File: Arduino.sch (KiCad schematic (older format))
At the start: 0 parts

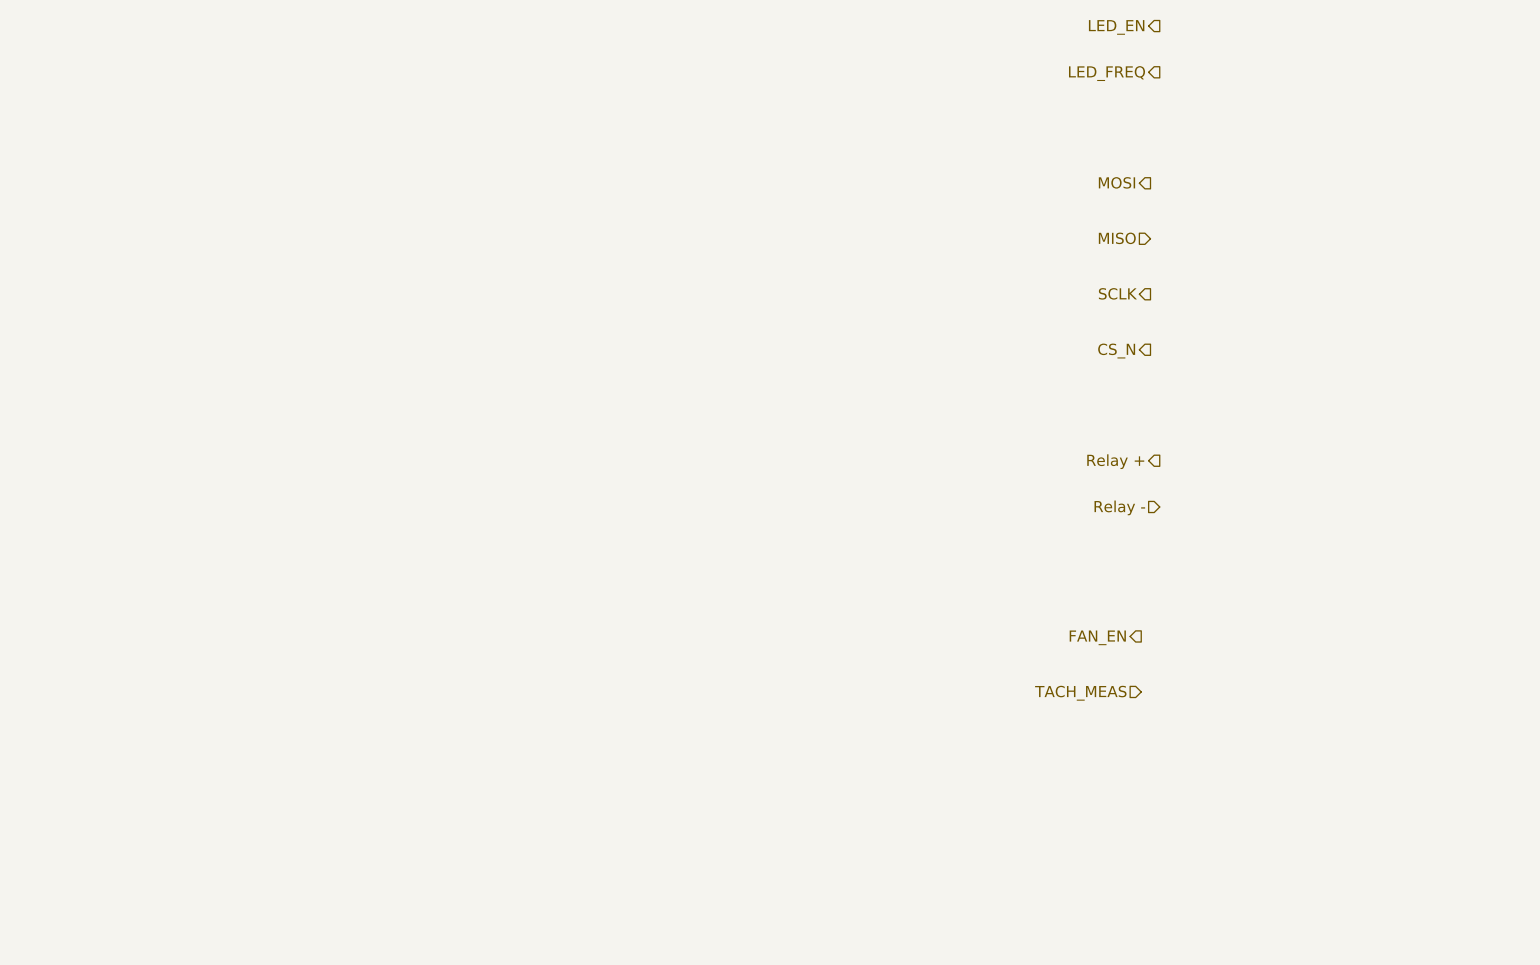
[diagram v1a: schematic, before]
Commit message: M3 U8
Arduino Module.   My Arduino Pin numbering does not matches Chris'.  I
believe he missed one in the video
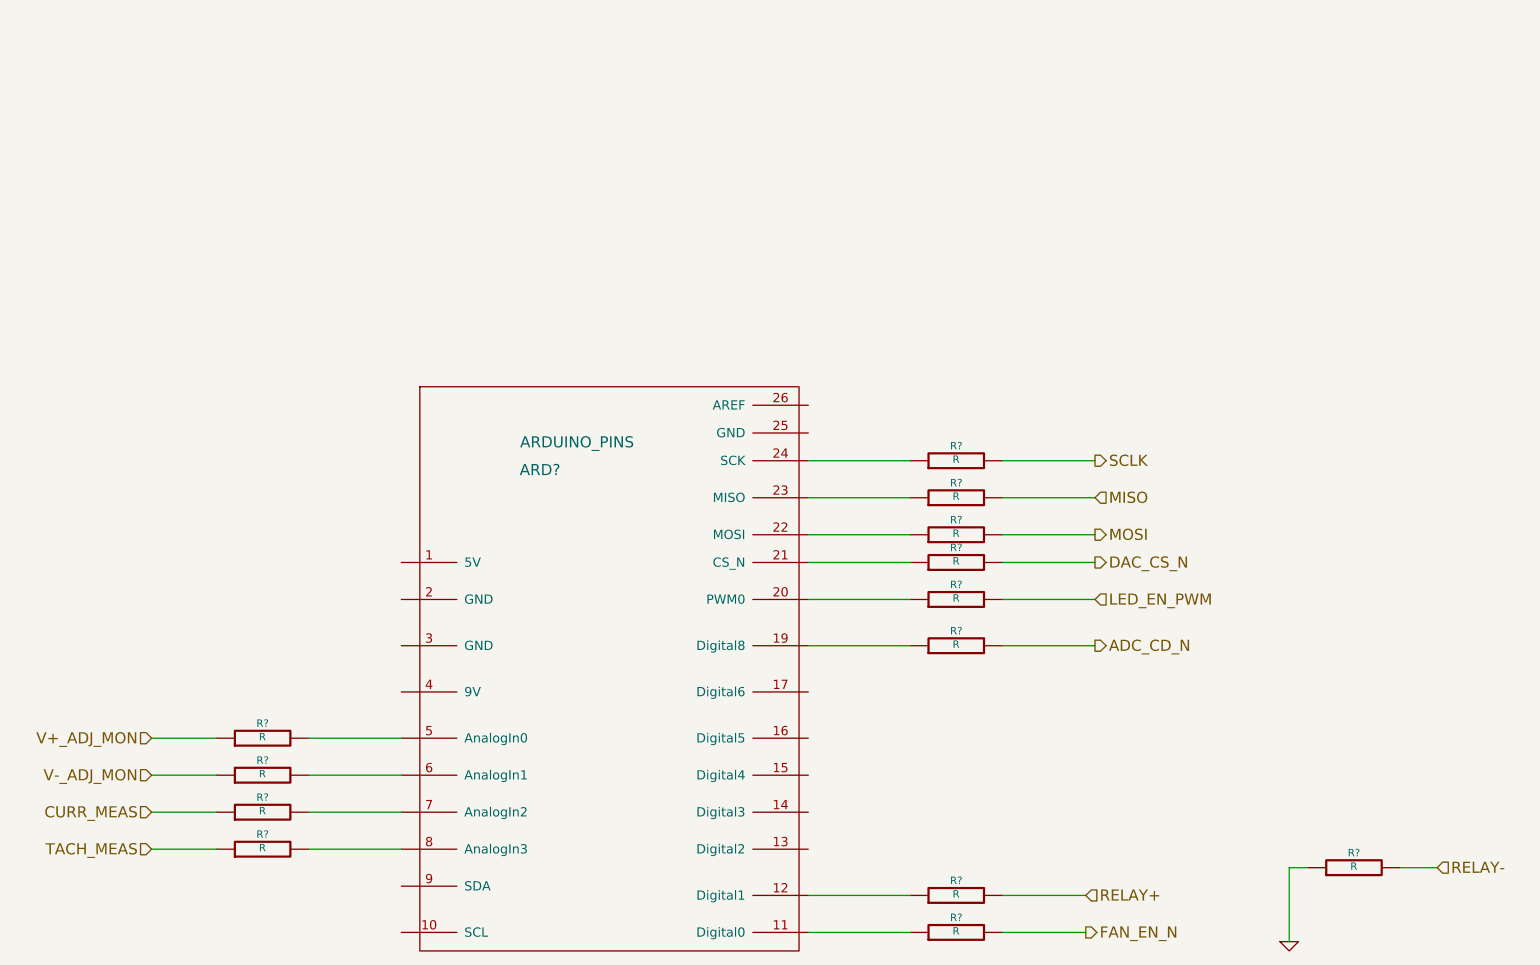
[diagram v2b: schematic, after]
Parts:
- added ARD?: ARDUINO_PINS, symbol ARDUINO_PINS
- added R? (x13): R, ~, symbol R
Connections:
- net MISO: now also R?.2
- net MOSI: now also R?.2
- net SCLK: now also R?.2
- net TACH_MEAS: now also R?.1
- new net: ARD?.11 (Digital0), R?.1
- new net: ARD?.12 (Digital1), R?.1
- new net: ARD?.19 (Digital8), R?.1
- new net: ARD?.20 (PWM0), R?.1
- new net: ARD?.21 (CS_N), R?.1
- new net: ARD?.22 (MOSI), R?.1
- new net: ARD?.23 (MISO), R?.1
- new net: ARD?.24 (SCK), R?.1
- new net: ARD?.5 (AnalogIn0), R?.2
- new net: ARD?.6 (AnalogIn1), R?.2
- new net: ARD?.7 (AnalogIn2), R?.2
- new net: ARD?.8 (AnalogIn3), R?.2
- new net ADC_CD_N: R?.2
- new net CURR_MEAS: R?.1
- new net DAC_CS_N: R?.2
- new net FAN_EN_N: R?.2
- new net GND: R?.1
- new net LED_EN_PWM: R?.2
- new net RELAY+: R?.2
- new net RELAY-: R?.2
- new net V+_ADJ_MON: R?.1
- new net V-_ADJ_MON: R?.1

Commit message: M3 U9
Revisiting the Current/Fan Module
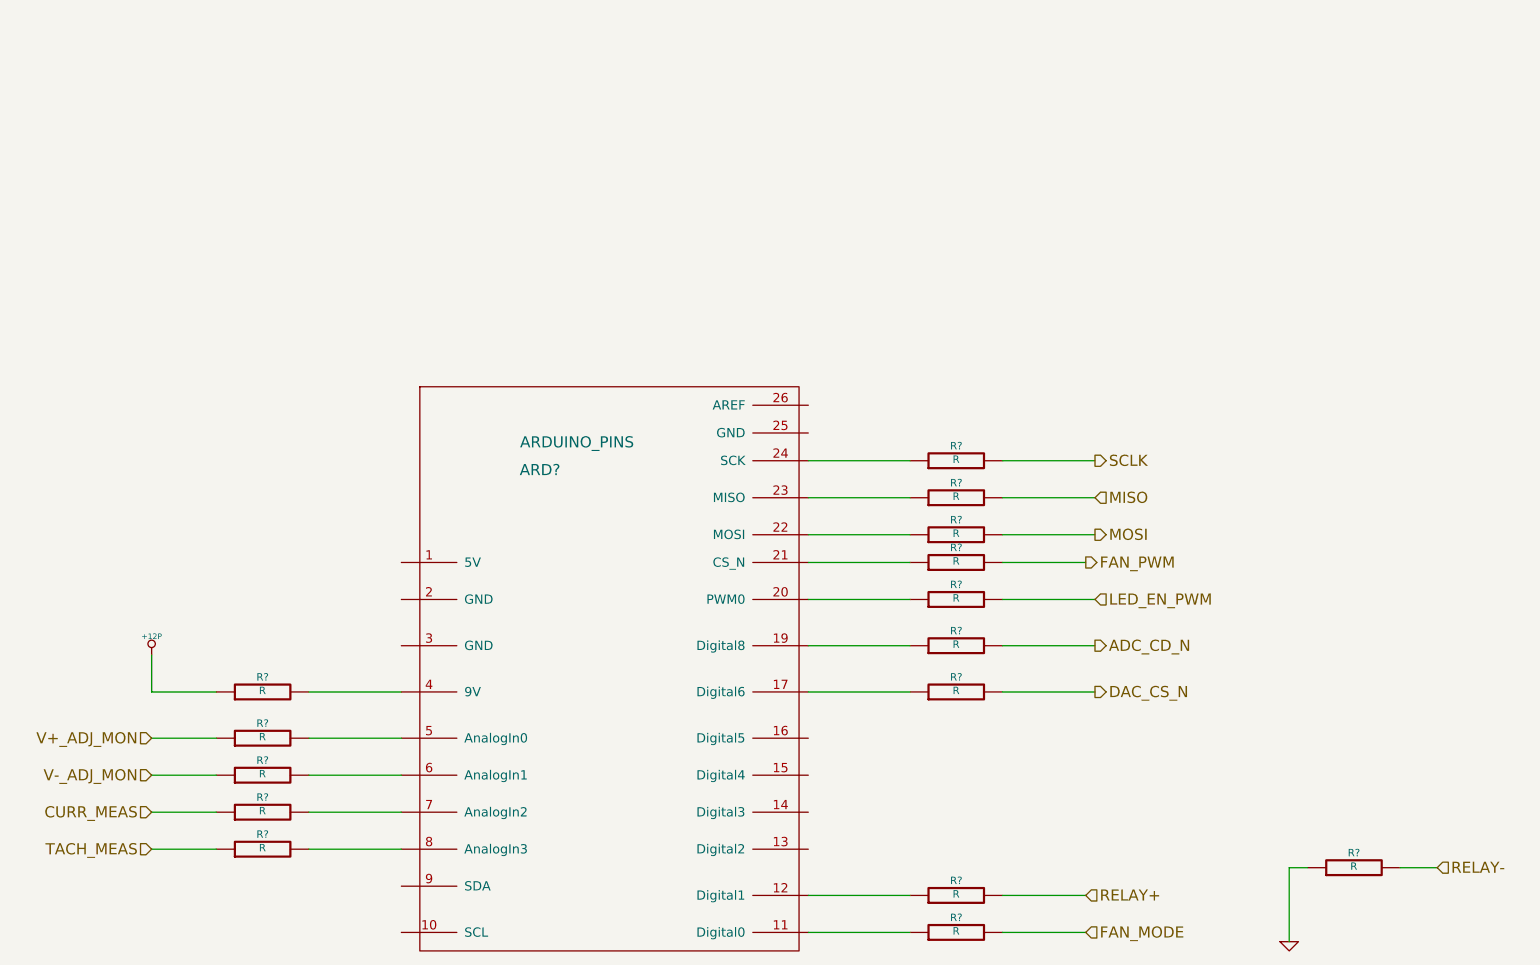
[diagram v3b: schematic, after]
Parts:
- added R? (x2): R, ~, symbol R
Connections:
- net at ARD?.11 (Digital0): now also R?.1; no longer R?.1
- net at ARD?.17 (Digital6): now also R?.1
- net at ARD?.21 (CS_N): now also R?.1; no longer R?.1
- net at ARD?.4 (9V): now also R?.2
- net FAN_EN_N renamed FAN_PWM
- new net +12P: R?.1
- new net FAN_MODE: R?.2
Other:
- moved on the sheet: R?
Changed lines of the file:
@@
 Text HLabel 6750 3850 2    60   Output ~ 0
 SCLK
-Text HLabel 6750 4400 2    60   Output ~ 0
+Text HLabel 6750 5100 2    60   Output ~ 0
 DAC_CS_N
-Text HLabel 6700 6400 2    60   Output ~ 0
-FAN_EN_N
+Text HLabel 6700 4400 2    60   Output ~ 0
+FAN_PWM
 Text HLabel 1650 5950 0    60   Input ~ 0
 TACH_MEAS
@@
 	6250 4250 6750 4250
 Wire Wire Line
-	6750 4400 6250 4400
+	6750 5100 6250 5100
 Wire Wire Line
 	3000 5950 2500 5950
@@
 L R R?
 U 1 1 52FEF63C
-P 6000 6400
-F 0 "R?" V 6080 6400 40  0000 C CNN
-F 1 "R" V 6007 6401 40  0000 C CNN
-F 2 "~" V 5930 6400 30  0000 C CNN
-F 3 "~" H 6000 6400 30  0000 C CNN
-	1    6000 6400
-	0    -1   -1   0
-$EndComp
-Wire Wire Line
-	6700 6400 6250 6400
-Wire Wire Line
-	5750 6400 5200 6400
+P 6000 4400
+F 0 "R?" V 6080 4400 40  0000 C CNN
+F 1 "R" V 6007 4401 40  0000 C CNN
+F 2 "~" V 5930 4400 30  0000 C CNN
+F 3 "~" H 6000 4400 30  0000 C CNN
+	1    6000 4400
+	0    -1   -1   0
+$EndComp
+Wire Wire Line
+	6700 4400 6250 4400
+Wire Wire Line
+	5750 4400 5200 4400
 $Comp
 L R R?
@@
 L R R?
 U 1 1 52FF6371
-P 6000 4400
-F 0 "R?" V 6080 4400 40  0000 C CNN
-F 1 "R" V 6007 4401 40  0000 C CNN
-F 2 "~" V 5930 4400 30  0000 C CNN
-F 3 "~" H 6000 4400 30  0000 C CNN
-	1    6000 4400
+P 6000 5100
+F 0 "R?" V 6080 5100 40  0000 C CNN
+F 1 "R" V 6007 5101 40  0000 C CNN
+F 2 "~" V 5930 5100 30  0000 C CNN
+F 3 "~" H 6000 5100 30  0000 C CNN
+	1    6000 5100
 	0    -1   -1   0
 $EndComp
@@
 	5750 4250 5200 4250
 Wire Wire Line
-	5200 4400 5750 4400
+	5200 5100 5750 5100
 $Comp
 L R R?
@@
 Wire Wire Line
 	5750 4850 5200 4850
+Text HLabel 6700 6400 2    60   Input ~ 0
+FAN_MODE
+$Comp
+L R R?
+U 1 1 53014B60
+P 6000 6400
+F 0 "R?" V 6080 6400 40  0000 C CNN
+F 1 "R" V 6007 6401 40  0000 C CNN
+F 2 "~" V 5930 6400 30  0000 C CNN
+F 3 "~" H 6000 6400 30  0000 C CNN
+	1    6000 6400
+	0    -1   -1   0
+$EndComp
+Wire Wire Line
+	5750 6400 5200 6400
+Wire Wire Line
+	6250 6400 6700 6400
+$Comp
+L R R?
+U 1 1 53014BAB
+P 2250 5100
+F 0 "R?" V 2330 5100 40  0000 C CNN
+F 1 "R" V 2257 5101 40  0000 C CNN
+F 2 "~" V 2180 5100 30  0000 C CNN
+F 3 "~" H 2250 5100 30  0000 C CNN
+	1    2250 5100
+	0    -1   -1   0
+$EndComp
+Wire Wire Line
+	2500 5100 3000 5100
+Wire Wire Line
+	2000 5100 1650 5100
+Wire Wire Line
+	1650 5100 1650 4900
+$Comp
+L +12P #PWR?
+U 1 1 53014C12
+P 1650 4900
+F 0 "#PWR?" H 1650 4870 30  0001 C CNN
+F 1 "+12P" H 1650 5000 30  0000 C CNN
+F 2 "" H 1650 4900 60  0000 C CNN
+F 3 "" H 1650 4900 60  0000 C CNN
+	1    1650 4900
+	1    0    0    -1
+$EndComp
 $EndSCHEMATC
